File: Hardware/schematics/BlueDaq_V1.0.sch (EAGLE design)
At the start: 59 parts, among them IC1 MEGA8-AI, Q1 MMBT2222, Q2 MMBT2222, Q3 MMBT2222, Q4 MMBT2222, U1 MCP73831, U2 TPS61200, U3 BME280, U4 MIC5225-3.3, X1 USB-MICROB, X2 3.5mm, X3 RELAY_LATCHINGEE2NUH, X4 3.5mm, X5 RELAY_LATCHINGEE2NUH, Y1 16 mhz

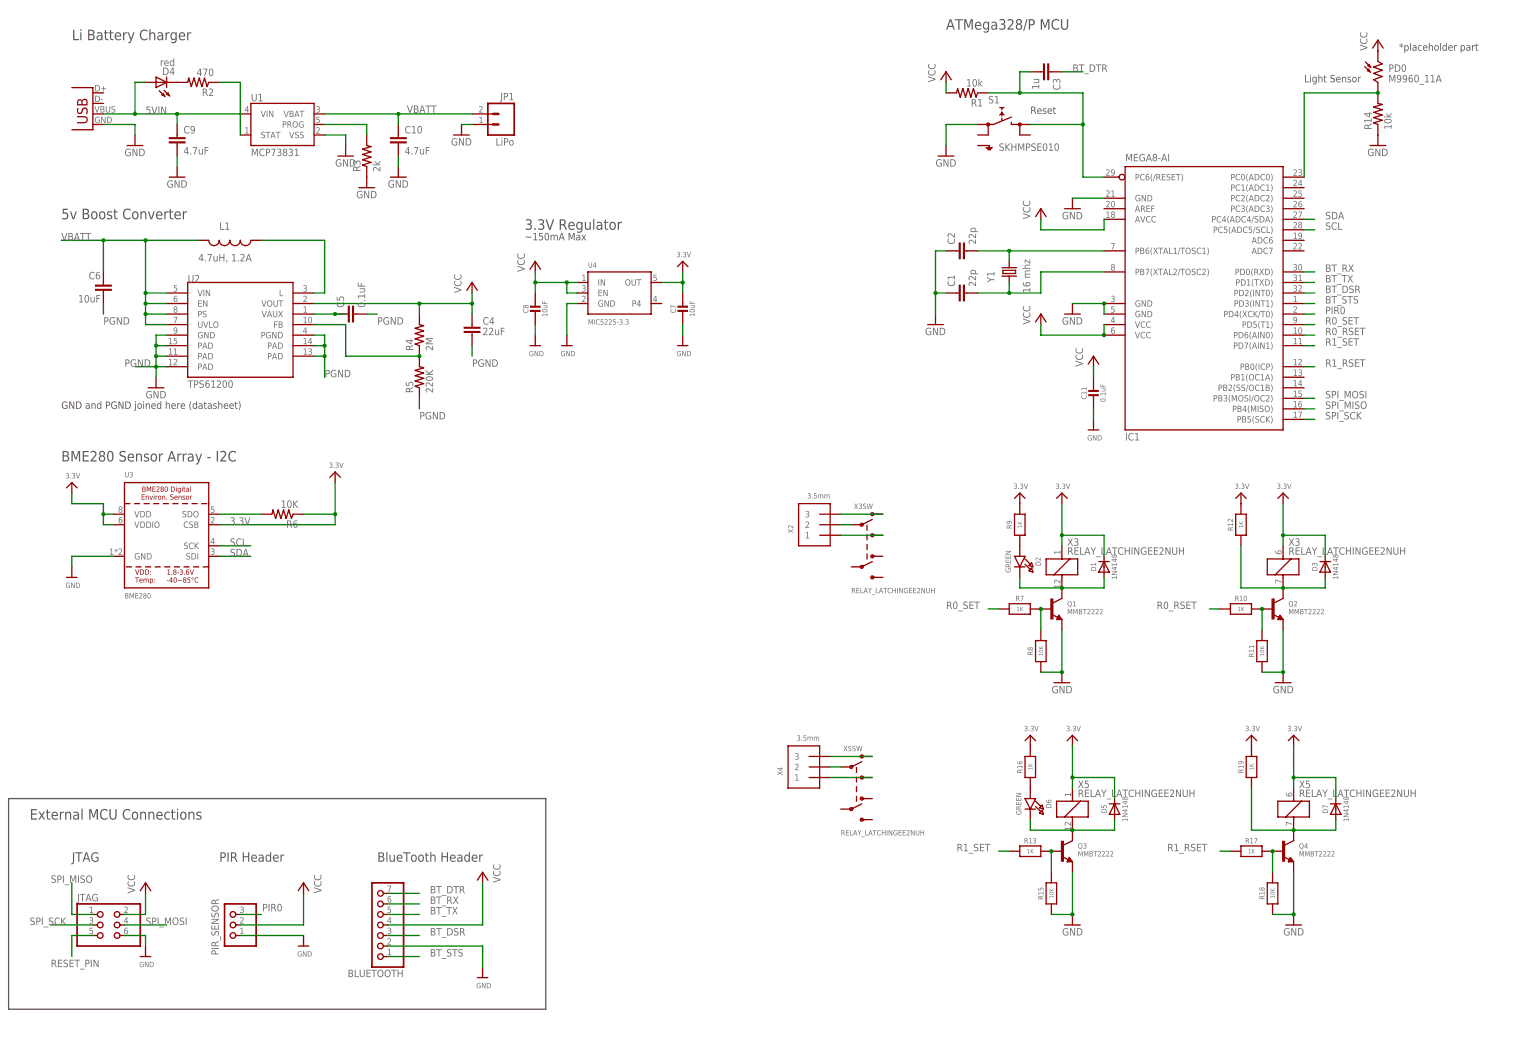
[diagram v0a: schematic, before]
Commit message: + Design meets DRC
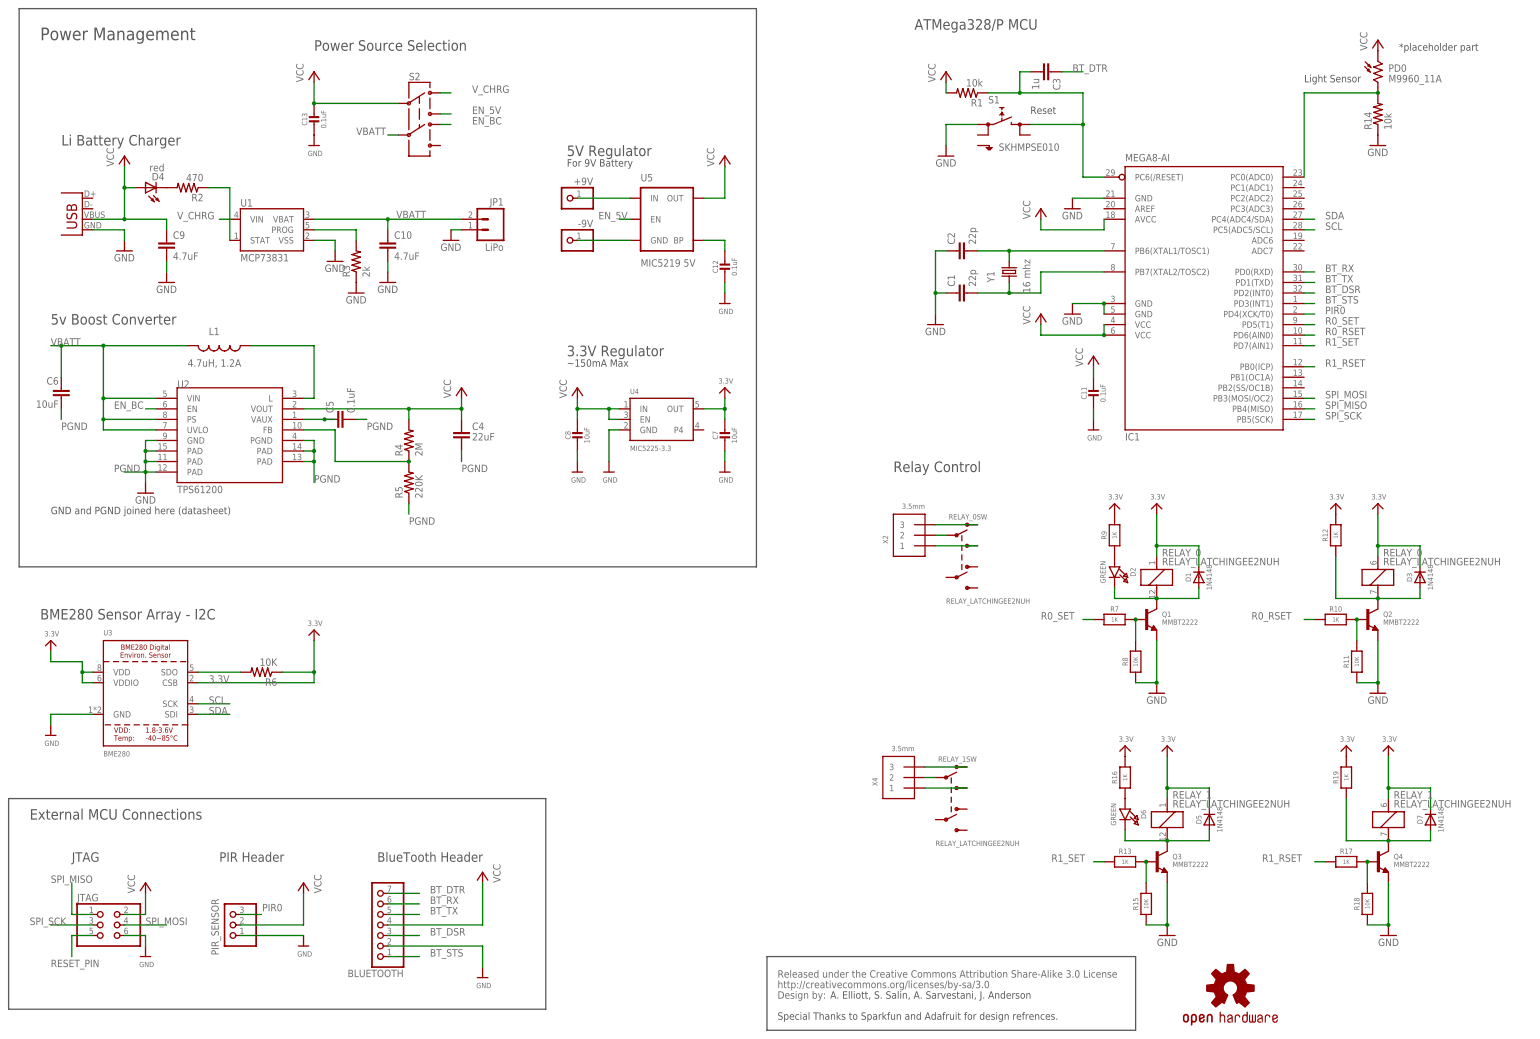
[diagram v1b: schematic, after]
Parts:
- removed X3, X5: RELAY_LATCHINGEE2NUH, microbuilder:RELAY_LATCHINGEE2NUH
- added +9V, -9V: (no value), adafruit:PINHD-1X1
- added C12, C13: 0.1uF, microbuilder:CAP_CERAMIC0805-NOOUTLINE
- added RELAY_0, RELAY_1: RELAY_LATCHINGEE2NUH, microbuilder:RELAY_LATCHINGEE2NUH
- added S2: (no value), SparkFun-Electromechanical:SWITCH-DPDTEG2211
- added U$22: OSHW-LOGOS, SparkFun:OSHW-LOGOS
- added U$23: CREATIVE_COMMONS, SparkFun-Aesthetics:CREATIVE_COMMONS
- added U5: MIC5219 5V, SparkFun-PowerIC:V_REG_MIC52195V
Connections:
- removed net 5VIN: C9.1, D4.A, U1.VIN, X1.VBUS
- new net EN_5V: S2.3, U5.EN
- new net EN_BC: S2.4, U2.EN
- new net N$15: +9V.1, U5.IN
- new net N$16: -9V.1, U5.GND
- new net N$17: C12.1, U5.BP
- new net V_CHRG: S2.1, U1.VIN
- net 3.3V: now also RELAY_0RESET.1, RELAY_0SET.1, RELAY_1RESET.1, RELAY_1SET.1; no longer X3RESET.1, X3SET.1, X5RESET.1, X5SET.1
- net COM1: now also RELAY_0SW.P1; no longer X3SW.P1
- net COM2: now also RELAY_1SW.P1; no longer X5SW.P1
- net GND: now also C12.2, C13.2
- net N$10: now also RELAY_1SW.O1; no longer X5SW.O1
- net N$12: now also RELAY_1RESET.2; no longer X5RESET.2
- net N$25: now also RELAY_0RESET.2; no longer X3RESET.2
- net N$28: now also RELAY_0SW.O1; no longer X3SW.O1
- net N$6: now also RELAY_0SET.2; no longer X3SET.2
- net N$7: now also RELAY_1SET.2; no longer X5SET.2
- net NO1: now also RELAY_0SW.S1; no longer X3SW.S1
- net NO2: now also RELAY_1SW.S1; no longer X5SW.S1
- net VBATT: now also S2.5; no longer U2.EN
- net VCC: now also C13.1, C9.1, D4.A, S2.2, U5.OUT, X1.VBUS
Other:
- note added: "5V Regulator"
- note added: "A. Elliott, S. Salin, A. Sarvestani, J. Anderson"
- note added: "For 9V Battery"
- note added: "Power Management"
- note added: "Power Source Selection"
- note added: "Relay Control"
- note added: "Special Thanks to Sparkfun and Adafruit for design refrences."
- note added: "Z:/Documents/School/ECE 411 & Capstone/BlueDaq Logo.bmp"
- moved on the sheet: C10, C4, C5, C6, C7, C8, C9, D1, D2, D3, D4, D5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
